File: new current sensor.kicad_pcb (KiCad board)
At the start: 2 copper layers, 151.3 x 62.3 mm, 51 parts, among them J1 Conn_01x04, U1 ACS711xEXLT-31AB, U2 ACS711xEXLT-31AB, U3 ACS711xEXLT-31AB, U4 ACS711xEXLT-31AB, U5 ACS711xEXLT-31AB, U6 ACS711xEXLT-31AB, U7 ADS1119IPWR, U8 ADS1119IPWR

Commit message: mounting holes mounting holes
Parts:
- added REF**: MountingHole_3.7mm_Pad, MountingHole:MountingHole_3.7mm_Pad, F.Cu at (108.8, 87.8)
- added REF**: MountingHole_3.7mm_Pad, MountingHole:MountingHole_3.7mm_Pad, F.Cu at (247.8, 87.8)
- added REF**: MountingHole_3.7mm_Pad, MountingHole:MountingHole_3.7mm_Pad, F.Cu at (247.6, 37.7)
- added REF**: MountingHole_3.7mm_Pad, MountingHole:MountingHole_3.7mm_Pad, F.Cu at (108.5, 37.7)
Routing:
- net +3.3V: track 243.1 -> 242.4 mm
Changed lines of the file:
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@@
     )
+  )
+  (footprint "MountingHole:MountingHole_3.7mm_Pad" (layer "F.Cu")
+    (at 108.755052 87.833338)
+    (descr "Mounting Hole 3.7mm")
+    (tags "mounting hole 3.7mm")
+    (attr exclude_from_pos_files exclude_from_bom)
+    (fp_text reference "REF**" (at 0 -4.7) (layer "F.SilkS")
+      (effects (font (size 1 1) (thickness 0.15)))
+    )
+    (fp_text value "MountingHole_3.7mm_Pad" (at 0 4.7) (layer "F.Fab")
+      (effects (font (size 1 1) (thickness 0.15)))
+    )
+    (fp_text user "${REFERENCE}" (at 0 0) (layer "F.Fab")
+      (effects (font (size 1 1) (thickness 0.15)))
+    )
+    (fp_circle (center 0 0) (end 3.7 0) (layer "Cmts.User") (width 0.15) (fill none))
+    (fp_circle (center 0 0) (end 3.95 0) (layer "F.CrtYd") (width 0.05) (fill none))
+    (pad "1" thru_hole circle (at 0 0) (size 7.4 7.4) (drill 3.7) (layers *.Cu *.Mask))
   )
   (footprint "Capacitor_SMD:C_0805_2012Metric_Pad1.18x1.45mm_HandSolder" (layer "F.Cu")
@@
     )
   )
+  (footprint "MountingHole:MountingHole_3.7mm_Pad" (layer "F.Cu")
+    (at 247.8 87.8)
+    (descr "Mounting Hole 3.7mm")
+    (tags "mounting hole 3.7mm")
+    (attr exclude_from_pos_files exclude_from_bom)
+    (fp_text reference "REF**" (at 0 -4.7) (layer "F.SilkS")
+      (effects (font (size 1 1) (thickness 0.15)))
+    )
+    (fp_text value "MountingHole_3.7mm_Pad" (at 0 4.7) (layer "F.Fab")
+      (effects (font (size 1 1) (thickness 0.15)))
+    )
+    (fp_text user "${REFERENCE}" (at 0 0) (layer "F.Fab")
+      (effects (font (size 1 1) (thickness 0.15)))
+    )
+    (fp_circle (center 0 0) (end 3.7 0) (layer "Cmts.User") (width 0.15) (fill none))
+    (fp_circle (center 0 0) (end 3.95 0) (layer "F.CrtYd") (width 0.05) (fill none))
+    (pad "1" thru_hole circle (at 0 0) (size 7.4 7.4) (drill 3.7) (layers *.Cu *.Mask))
+  )
   (footprint "Capacitor_SMD:C_0805_2012Metric_Pad1.18x1.45mm_HandSolder" (layer "F.Cu")
     (at 173.4375 56.6)
@@
     )
   )
+  (footprint "MountingHole:MountingHole_3.7mm_Pad" (layer "F.Cu")
+    (at 247.6 37.7)
+    (descr "Mounting Hole 3.7mm")
+    (tags "mounting hole 3.7mm")
+    (attr exclude_from_pos_files exclude_from_bom)
+    (fp_text reference "REF**" (at 0 -4.7) (layer "F.SilkS")
+      (effects (font (size 1 1) (thickness 0.15)))
+    )
+    (fp_text value "MountingHole_3.7mm_Pad" (at 0 4.7) (layer "F.Fab")
+      (effects (font (size 1 1) (thickness 0.15)))
+    )
+    (fp_text user "${REFERENCE}" (at 0 0) (layer "F.Fab")
+      (effects (font (size 1 1) (thickness 0.15)))
+    )
+    (fp_circle (center 0 0) (end 3.7 0) (layer "Cmts.User") (width 0.15) (fill none))
+    (fp_circle (center 0 0) (end 3.95 0) (layer "F.CrtYd") (width 0.05) (fill none))
+    (pad "1" thru_hole circle (at 0 0) (size 7.4 7.4) (drill 3.7) (layers *.Cu *.Mask))
+  )
   (footprint "Connector_Wire:SolderWire-0.25sqmm_1x01_D0.65mm_OD2mm" (layer "F.Cu")
     (at 137.5 74.9 -90)
@@
       (rotate (xyz 0 0 0))
     )
+  )
+  (footprint "MountingHole:MountingHole_3.7mm_Pad" (layer "F.Cu")
+    (at 108.5 37.7)
+    (descr "Mounting Hole 3.7mm")
+    (tags "mounting hole 3.7mm")
+    (attr exclude_from_pos_files exclude_from_bom)
+    (fp_text reference "REF**" (at 0 -4.7) (layer "F.SilkS")
+      (effects (font (size 1 1) (thickness 0.15)))
+    )
+    (fp_text value "MountingHole_3.7mm_Pad" (at 0 4.7) (layer "F.Fab")
+      (effects (font (size 1 1) (thickness 0.15)))
+    )
+    (fp_text user "${REFERENCE}" (at 0 0) (layer "F.Fab")
+      (effects (font (size 1 1) (thickness 0.15)))
+    )
+    (fp_circle (center 0 0) (end 3.7 0) (layer "Cmts.User") (width 0.15) (fill none))
+    (fp_circle (center 0 0) (end 3.95 0) (layer "F.CrtYd") (width 0.05) (fill none))
+    (pad "1" thru_hole circle (at 0 0) (size 7.4 7.4) (drill 3.7) (layers *.Cu *.Mask))
   )
   (footprint "Capacitor_SMD:C_0805_2012Metric_Pad1.18x1.45mm_HandSolder" (layer "F.Cu")
@@
   (segment (start 224.155 60.325) (end 217.725 60.325) (width 0.25) (layer "B.Cu") (net 1))
   (segment (start 198.2 61.3) (end 194.2 61.3) (width 0.25) (layer "B.Cu") (net 1))
-  (segment (start 212.25 61.75) (end 211.7 61.2) (width 0.25) (layer "B.Cu") (net 1))
   (segment (start 227.33 60.5755) (end 227.0795 60.325) (width 0.25) (layer "B.Cu") (net 1))
   (segment (start 215.4 64.9) (end 212.25 61.75) (width 0.25) (layer "B.Cu") (net 1))

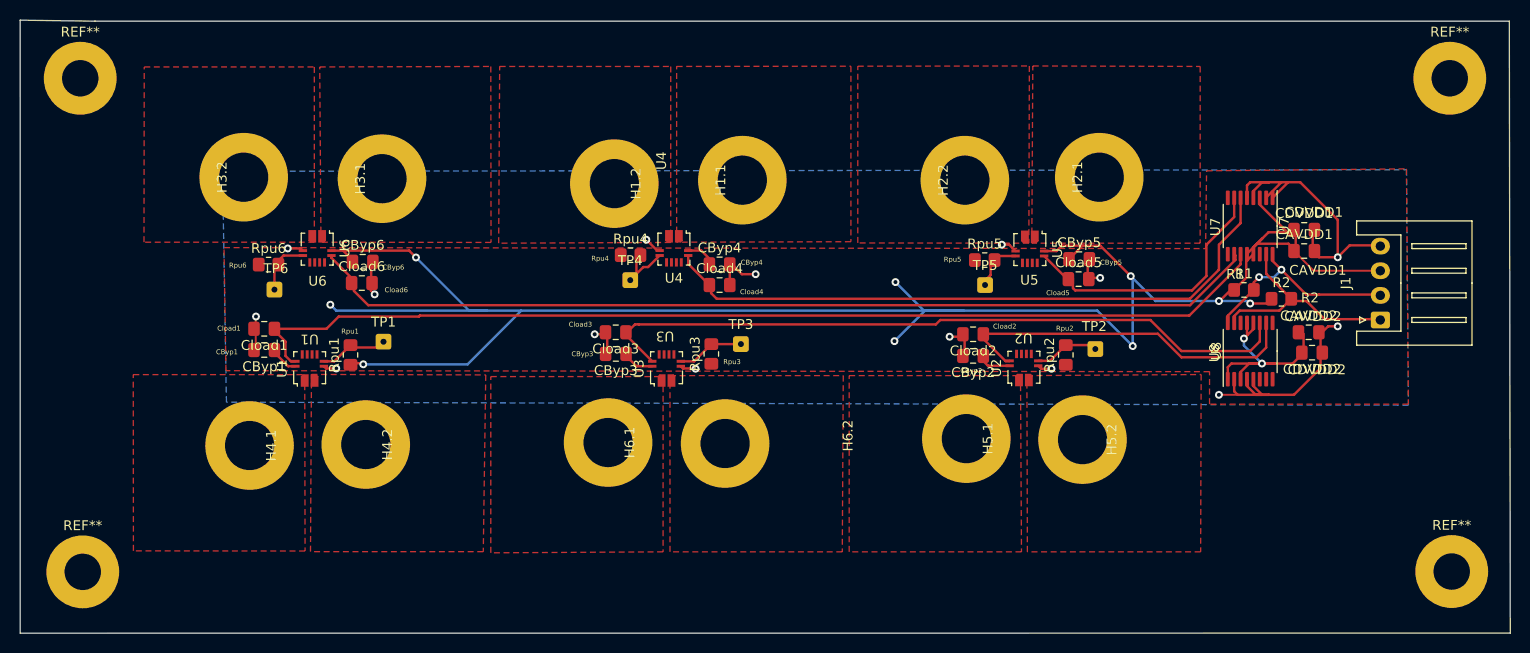
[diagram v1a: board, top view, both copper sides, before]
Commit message: Reference pad update
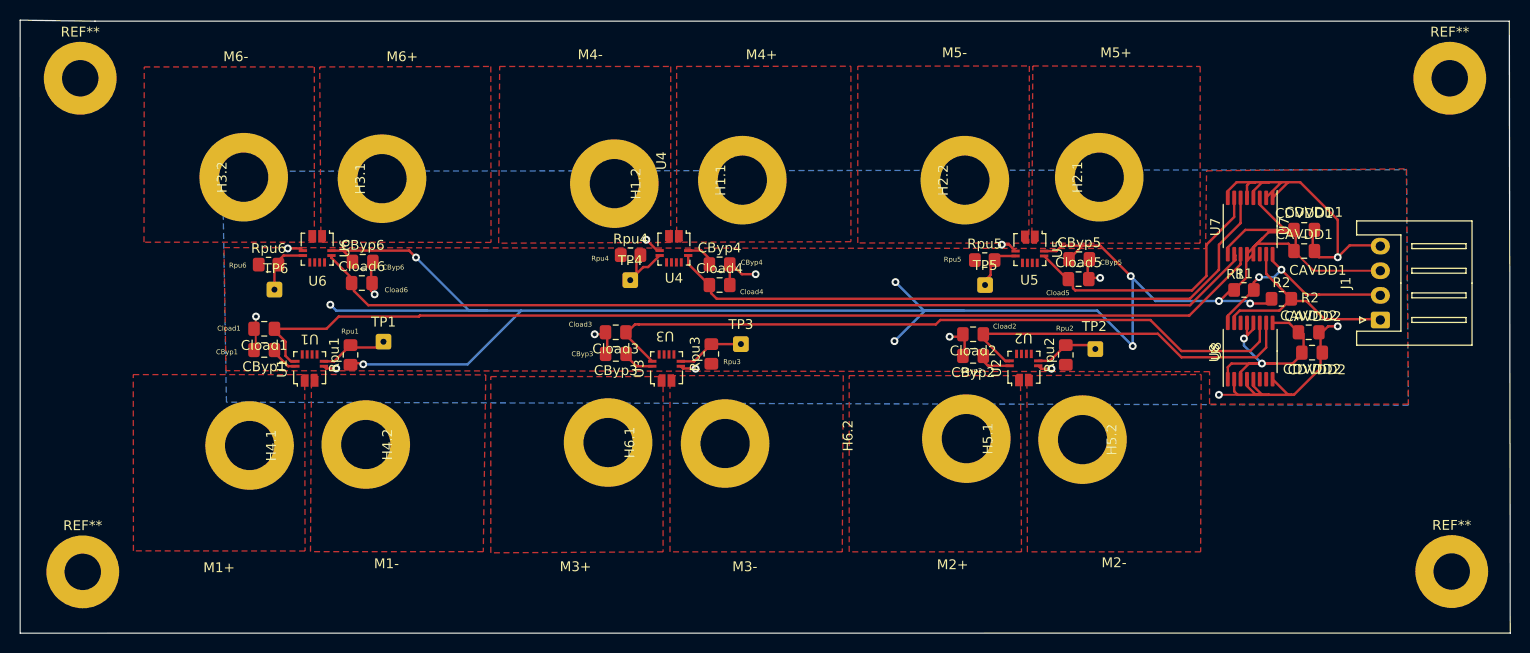
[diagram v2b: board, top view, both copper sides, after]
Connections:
- U7 pad 8: unconnected-(U7-Pad8) -> Earth
- U7 pad 9: unconnected-(U7-Pad9) -> +3.3V
- U8 pad 8: unconnected-(U8-Pad8) -> Earth
- U8 pad 9: unconnected-(U8-Pad9) -> +3.3V
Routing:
- net +3.3V: track 242.4 -> 253.5 mm
- net Earth: track 89.2 -> 95.7 mm
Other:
- board text added: "M1+"
- board text added: "M1-"
- board text added: "M2+"
- board text added: "M2-"
- board text added: "M3+"
- board text added: "M3-"
- board text added: "M4+"
- board text added: "M4-"
- board text added: "M5+"
- board text added: "M5-"
- board text added: "M6+"
- board text added: "M6-"

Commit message: midway point
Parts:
- added CAVDDRP1: 0.1, Capacitor_SMD:C_0805_2012Metric_Pad1.18x1.45mm_HandSolder, F.Cu at (228.7, 75.2)
- added CAVDDRP2: 0.1, Capacitor_SMD:C_0805_2012Metric_Pad1.18x1.45mm_HandSolder, F.Cu at (228.1, 43.5)
- moved CAVDD2 13.4 mm to (226.6, 75.2), turned to -90 degrees
- moved CDVDD2 13.2 mm to (224.5, 75.2), turned to 90 degrees
- moved CDVDD1 12.1 mm to (225.4, 43.5), turned to 90 degrees
- moved CAVDD1 11.8 mm to (230.8, 43.6), turned to 90 degrees
- moved U8 3.23 mm to (227.4, 68.6), turned to -90 degrees
- moved U7 1.78 mm to (227.1, 50.9), turned to 90 degrees
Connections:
- J1 pad 3: +3.3V -> +3V3
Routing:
- net +3.3V: track 253.5 -> 185.5 mm, vias 11 -> 9
- net Earth: track 95.7 -> 62.8 mm, vias 15 -> 22
- net Net-(Cload4-Pad1): track 66.6 -> 50.9 mm
- net Net-(Cload5-Pad1): track 28.1 -> 12.5 mm
- net Net-(Cload2-Pad1): track 36.6 -> 25.1 mm
- net Net-(Cload3-Pad1): track 72.7 -> 62.5 mm
- net +3V3: track 0.00 -> 9.53 mm
- net Net-(Cload1-Pad1): track 106.4 -> 98.0 mm
- net Net-(J1-Pad1): track 22.5 -> 15.0 mm
- net Net-(Cload6-Pad1): track 97.2 -> 90.1 mm
- net Net-(J1-Pad2): track 21.4 -> 16.3 mm

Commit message: 3/26 ready for revision
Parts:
- moved R2 4.97 mm to (235.5, 59.7), turned to 180 degrees
- moved R1 3.71 mm to (230.4, 59.7)
- moved J1 3.30 mm to (243.8, 62.1)
- moved CAVDDRP1 2.24 mm to (230.9, 75.1)
- moved CAVDD2 2.24 mm to (228.8, 75.1)
- moved CDVDD2 2.24 mm to (226.7, 75.1)
- moved U8 1.48 mm to (228.9, 68.6)
- moved U7 1.44 mm to (228.6, 51.0)
- moved CAVDD1 0.74 mm to (230.3, 43.1)
- moved CDVDD1 0.65 mm to (224.9, 43.1)
- moved CAVDDRP2 0.65 mm to (227.6, 43.1)
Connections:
- J1 pad 3: +3V3 -> +3.3V
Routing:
- net Net-(Cload6-Pad1): track 90.1 -> 115.5 mm, vias 0 -> 2
- net Net-(Cload1-Pad1): track 98.0 -> 122.5 mm, vias 0 -> 2
- net Net-(J1-Pad2): track 16.3 -> 40.7 mm
- net Net-(J1-Pad1): track 15.0 -> 38.8 mm, vias 0 -> 2
- net Net-(Cload5-Pad1): track 12.5 -> 29.1 mm, vias 0 -> 2
- net Net-(Cload4-Pad1): track 50.9 -> 66.0 mm
- net Net-(Cload3-Pad1): track 62.5 -> 73.7 mm
- net Net-(Cload2-Pad1): track 25.1 -> 35.3 mm
- net +3V3: track 9.53 -> 0.00 mm
- net Earth: track 62.8 -> 60.1 mm, vias 22 -> 24
- net +3.3V: track 185.5 -> 184.6 mm, vias 9 -> 11
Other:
- board text added: "C1-3"
- board text added: "C4-6"
- board text removed: "CAVDD1"
- board text removed: "CAVDD2"
- board text removed: "CDVDD1"
- board text removed: "CDVDD2"

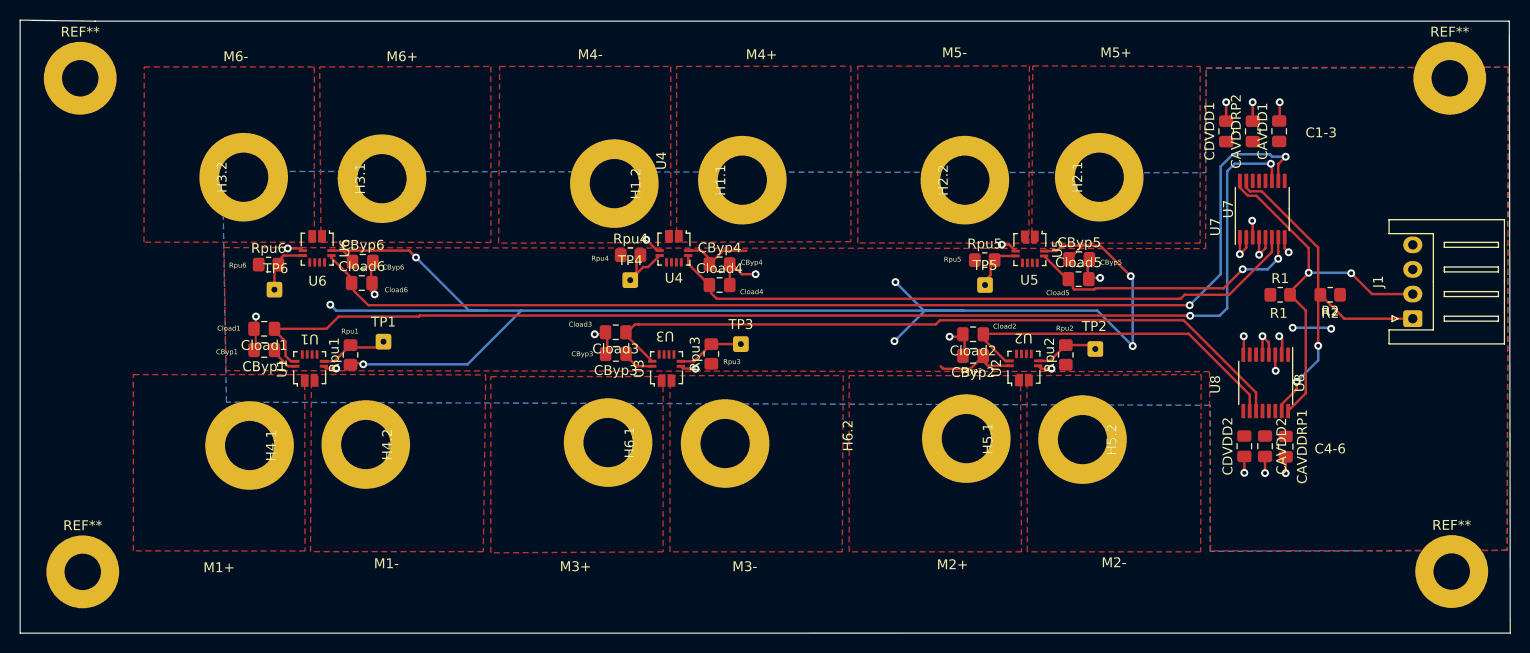
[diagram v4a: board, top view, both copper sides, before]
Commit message: added a 3.3v plane to the back
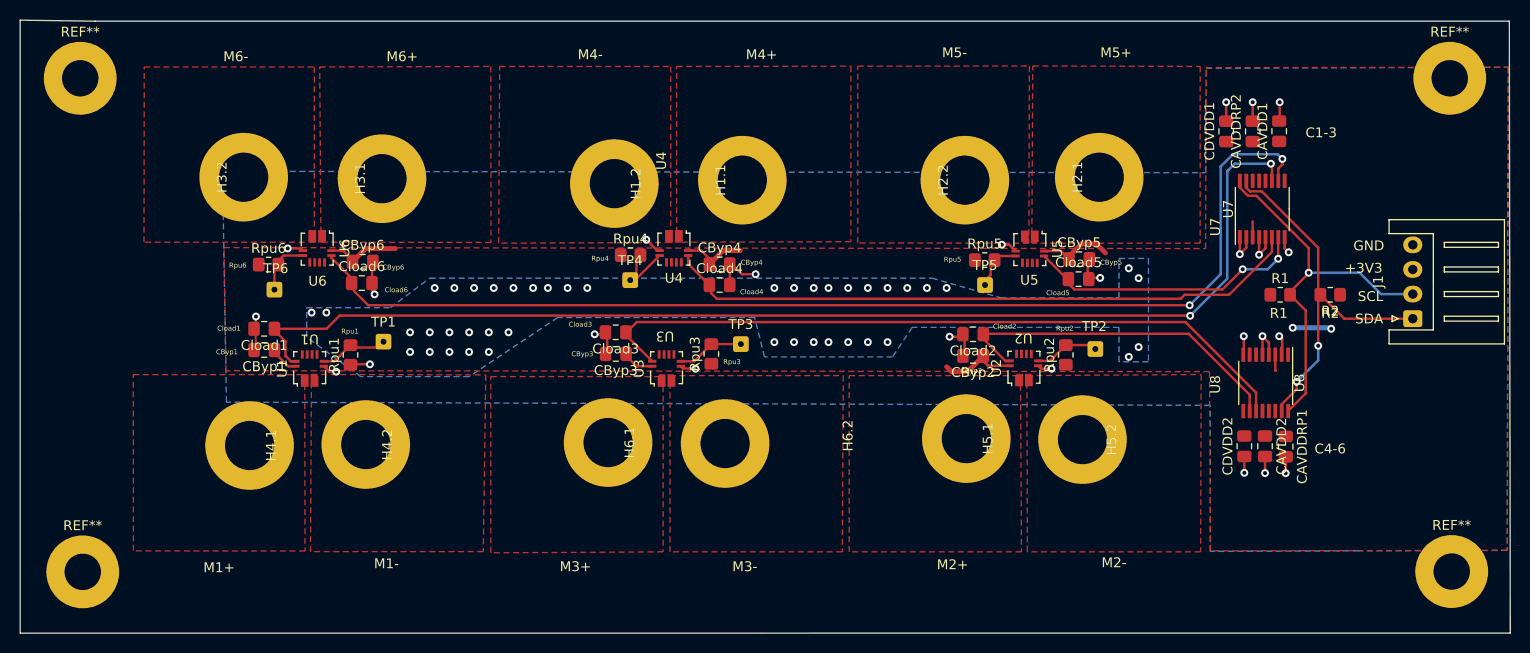
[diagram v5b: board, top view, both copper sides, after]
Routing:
- net +3.3V: track 184.6 -> 45.3 mm, vias 11 -> 46
- net Net-(Cload1-Pad1): track 122.5 -> 120.8 mm
- net Net-(Cload6-Pad1): track 115.5 -> 114.9 mm
- net Net-(J1-Pad2): vias 2 -> 1
- added copper zone on B.Cu, net +3.3V
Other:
- board text added: "+3V3"
- board text added: "GND"
- board text added: "SCL"
- board text added: "SDA"
